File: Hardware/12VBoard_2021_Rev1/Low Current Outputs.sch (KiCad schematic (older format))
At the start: 55 parts, among them Q10 IRLML2060, Q11 IRLML2060, Q12 IRLML2060, Q13 IRLML2060, U14 LT1910, U15 LT1910, U16 LT1910, U17 LT1910, U2 INA198, U4 LM2576S-12/NOPB, U9 OKI

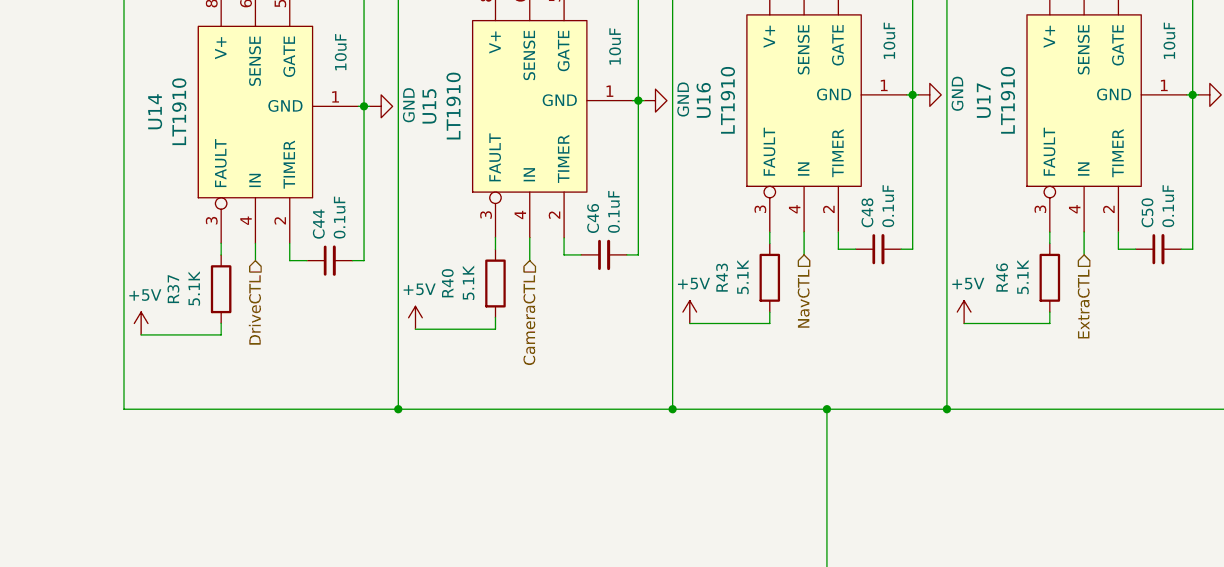
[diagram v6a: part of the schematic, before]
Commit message: changed to big bucks
changed to the bucks used in Master due to a realization in the inductor sizing for the LM5116. It would be much bigger than previous years.
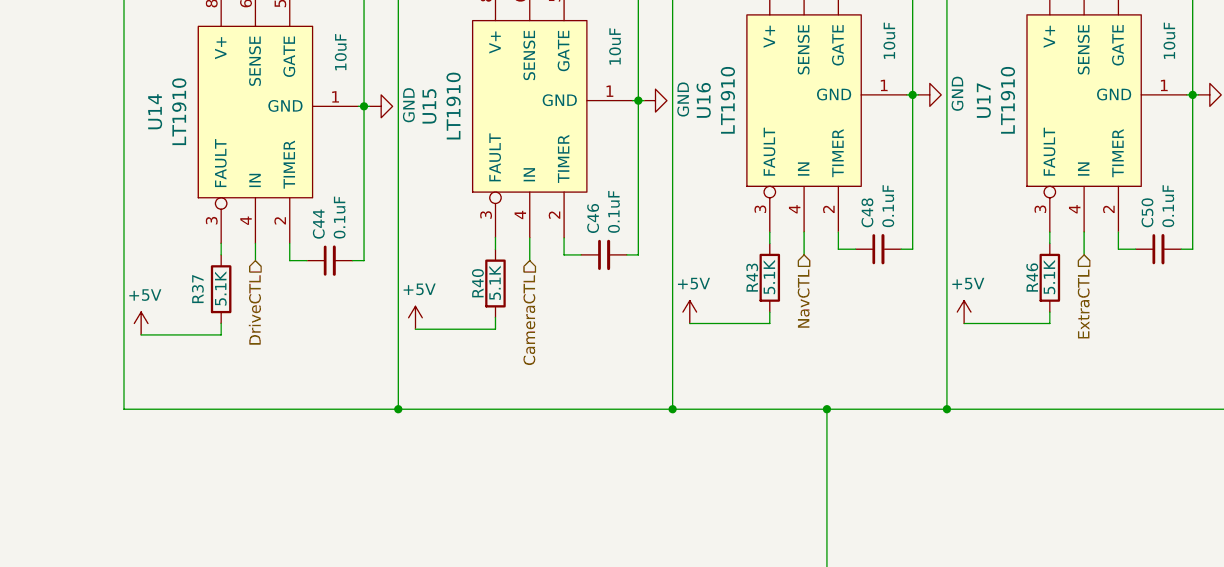
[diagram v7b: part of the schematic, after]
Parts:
- C4: footprint Capacitor_THT:CP_Radial_D12.5mm_P5.00mm -> Capacitor_THT:CP_Radial_D10.0mm_P5.00mm
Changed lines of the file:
@@
 $Descr A4 11693 8268
 encoding utf-8
-Sheet 8 9
+Sheet 8 8
 Title ""
 Date ""
@@
 F 0 "C4" V 4725 6525 50  0000 L CNN
 F 1 "1000 uF" V 4800 6450 50  0000 L CNN
-F 2 "Capacitor_THT:CP_Radial_D12.5mm_P5.00mm" H 4950 6575 50  0001 C CNN
+F 2 "Capacitor_THT:CP_Radial_D10.0mm_P5.00mm" H 4950 6575 50  0001 C CNN
 F 3 "~" H 4950 6575 50  0001 C CNN
 	1    4950 6575
@@
 AR Path="/5F74F36B/5F971CD6/5FC9854C" Ref="R?"  Part="1"
 AR Path="/5F74F223/5FC9854C" Ref="R43"  Part="1"
-F 0 "R43" V 5518 4175 50  0000 C CNN
-F 1 "5.1K" V 5609 4175 50  0000 C CNN
+F 0 "R43" V 5650 4175 50  0000 C CNN
+F 1 "5.1K" V 5725 4175 50  0000 C CNN
 F 2 "Resistor_SMD:R_0603_1608Metric_Pad1.05x0.95mm_HandSolder" V 5655 4175 50  0001 C CNN
 F 3 "~" H 5725 4175 50  0001 C CNN
@@
 AR Path="/5F74F36B/5F971CD6/5FDA95F6" Ref="R?"  Part="1"
 AR Path="/5F74F223/5FDA95F6" Ref="R37"  Part="1"
-F 0 "R37" V 3118 4225 50  0000 C CNN
-F 1 "5.1K" V 3209 4225 50  0000 C CNN
+F 0 "R37" V 3225 4225 50  0000 C CNN
+F 1 "5.1K" V 3325 4225 50  0000 C CNN
 F 2 "Resistor_SMD:R_0603_1608Metric_Pad1.05x0.95mm_HandSolder" V 3255 4225 50  0001 C CNN
 F 3 "~" H 3325 4225 50  0001 C CNN
@@
 AR Path="/5F74F36B/5F971CD6/5FDB0B63" Ref="R?"  Part="1"
 AR Path="/5F74F223/5FDB0B63" Ref="R40"  Part="1"
-F 0 "R40" V 4318 4200 50  0000 C CNN
-F 1 "5.1K" V 4409 4200 50  0000 C CNN
+F 0 "R40" V 4450 4200 50  0000 C CNN
+F 1 "5.1K" V 4525 4200 50  0000 C CNN
 F 2 "Resistor_SMD:R_0603_1608Metric_Pad1.05x0.95mm_HandSolder" V 4455 4200 50  0001 C CNN
 F 3 "~" H 4525 4200 50  0001 C CNN
@@
 AR Path="/5F74F36B/5F971CD6/5FDB8AD8" Ref="R?"  Part="1"
 AR Path="/5F74F223/5FDB8AD8" Ref="R46"  Part="1"
-F 0 "R46" V 6743 4175 50  0000 C CNN
-F 1 "5.1K" V 6834 4175 50  0000 C CNN
+F 0 "R46" V 6875 4175 50  0000 C CNN
+F 1 "5.1K" V 6950 4175 50  0000 C CNN
 F 2 "Resistor_SMD:R_0603_1608Metric_Pad1.05x0.95mm_HandSolder" V 6880 4175 50  0001 C CNN
 F 3 "~" H 6950 4175 50  0001 C CNN

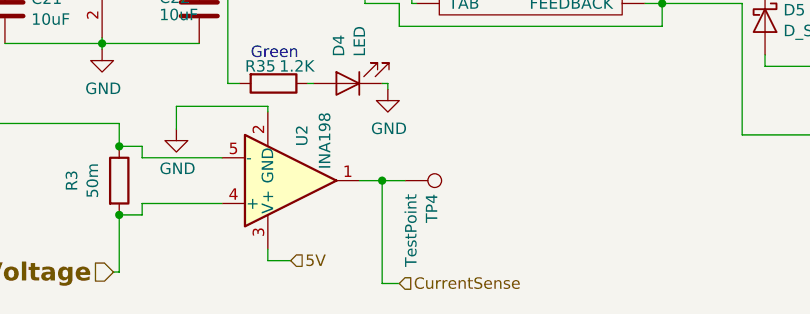
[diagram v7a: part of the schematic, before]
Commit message: admin changes
-current sensing on high current
-fixed traces for current sensing
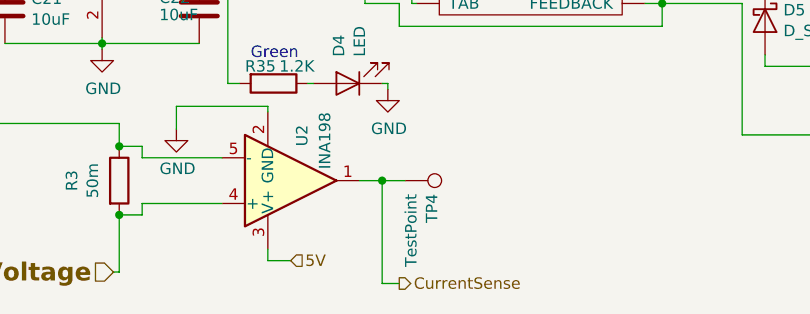
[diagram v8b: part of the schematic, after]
